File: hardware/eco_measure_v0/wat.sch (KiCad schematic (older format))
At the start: 31 parts

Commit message: desarrollando el hardware
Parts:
- removed C? (x6): 100nF, Capacitors_SMD:C_1206_HandSoldering, symbol wat-rescue:C
- removed D? (x2): D_Zener, symbol Device:D_Zener
- removed JP?: Jumper_2_Open, Jumper:SolderJumper-2_P1.3mm_Open_Pad1.0x1.5mm, symbol Jumper:Jumper_2_Open
- removed P?: PINZA_5, Connectors_Terminal_Blocks:TerminalBlock_bornier-2_P5.08mm, symbol wat-rescue:CONN_01X02
- removed P?: PINZA_6, Connectors_Terminal_Blocks:TerminalBlock_bornier-2_P5.08mm, symbol wat-rescue:CONN_01X02
- removed P?: PINZA_7, Connectors_Terminal_Blocks:TerminalBlock_bornier-2_P5.08mm, symbol wat-rescue:CONN_01X02
- removed P? (x2): PINZA_1, Connectors_Terminal_Blocks:TerminalBlock_bornier-2_P5.08mm, symbol wat-rescue:CONN_01X02
- removed P?: PINZA_2, Connectors_Terminal_Blocks:TerminalBlock_bornier-2_P5.08mm, symbol wat-rescue:CONN_01X02
- removed P?: PINZA_3, Connectors_Terminal_Blocks:TerminalBlock_bornier-2_P5.08mm, symbol wat-rescue:CONN_01X02
- removed P?: PINZA_4, Connectors_Terminal_Blocks:TerminalBlock_bornier-2_P5.08mm, symbol wat-rescue:CONN_01X02
- removed R? (x4): 10k, libreria_huellas_proyecto:Resistor_Horizontal_RM10mm, symbol wat-rescue:R
- removed R?: 2k2, libreria_huellas_proyecto:Resistor_Horizontal_RM10mm, symbol wat-rescue:R
- removed R?: 1k, libreria_huellas_proyecto:Resistor_Horizontal_RM10mm, symbol wat-rescue:R
- removed R?: 39, libreria_huellas_proyecto:Resistor_Horizontal_RM10mm, symbol wat-rescue:R
- removed R?: 10k, Resistors_SMD:R_1206_HandSoldering, symbol wat-rescue:R
- added C? (x16): 100nF, Capacitors_SMD:C_1206_HandSoldering, symbol wat-rescue:C
- added J? (x16): Conn_01x01, symbol Connector_Generic:Conn_01x01
- added R? (x26): 10k, libreria_huellas_proyecto:Resistor_Horizontal_RM10mm, symbol wat-rescue:R
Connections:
- net labels added: A0, D2
- net labels removed: 18b20_0, analogico_0, analogico_1, divisor_0, intensidad_1, lazo_0, pulsos_0, v_comun_0, v_comun_1, v_op, v_op_5v, v_referencia, voltage_1
- wire segments 127 -> 134
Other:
- moved on the sheet: C?, D?, J?, P?, U?, W?

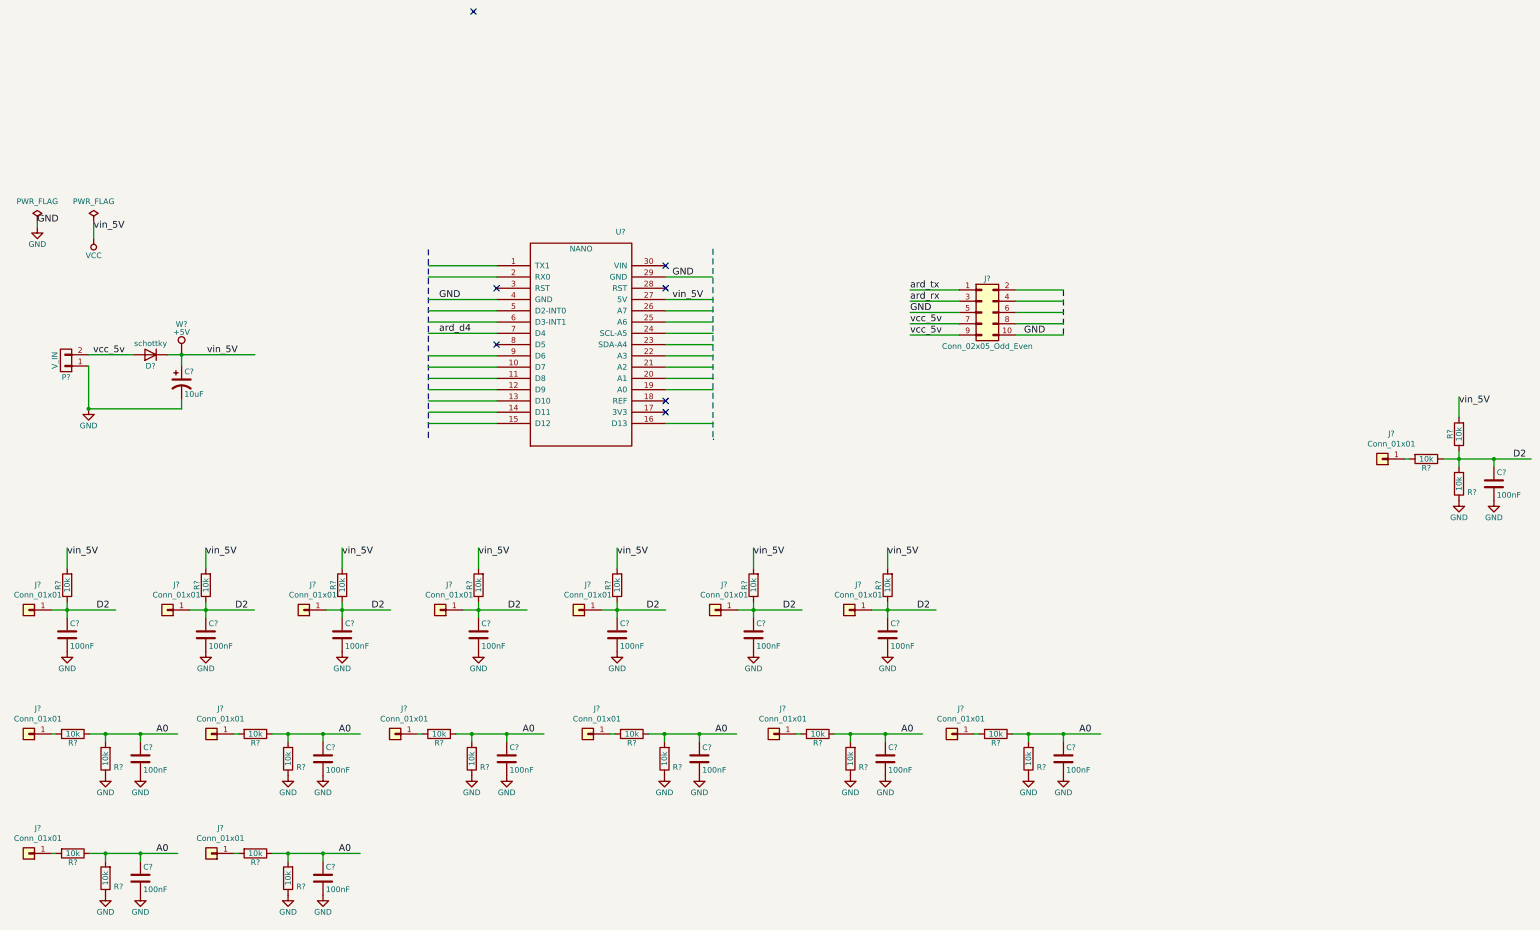
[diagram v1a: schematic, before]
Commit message: avanzando en la medida continua y la PCB
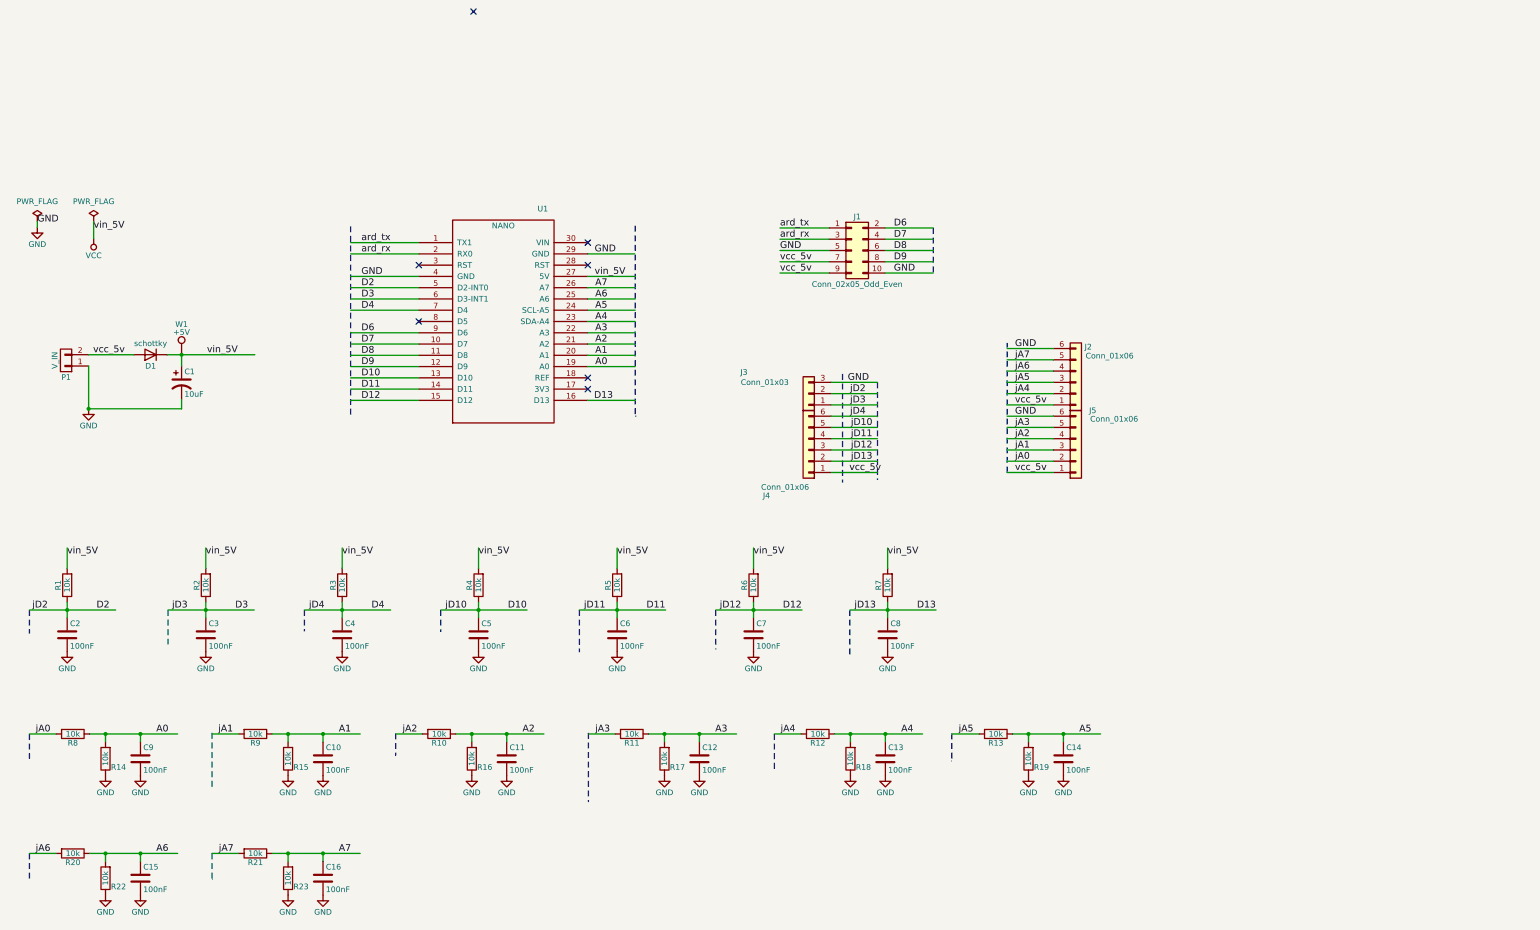
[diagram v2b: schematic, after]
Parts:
- removed C?: 100nF, Capacitors_SMD:C_1206_HandSoldering, symbol wat-rescue:C
- removed J? (x16): Conn_01x01, symbol Connector_Generic:Conn_01x01
- removed R? (x3): 10k, libreria_huellas_proyecto:Resistor_Horizontal_RM10mm, symbol wat-rescue:R
- added J2, J4, J5: Conn_01x06, TerminalBlock:TerminalBlock_bornier-6_P5.08mm, symbol Connector_Generic:Conn_01x06
- added J3: Conn_01x03, TerminalBlock:TerminalBlock_bornier-3_P5.08mm, symbol Connector_Generic:Conn_01x03
- C1: renamed from C?; footprint Capacitors_SMD:C_2220_HandSoldering -> eco_power_v2:C_2220_HandSoldering
- C10, C11, C12, C13, C14, C15, C16, C2, C3, C4, C5, C6, C7, C8, C9: renamed from C?; footprint Capacitors_SMD:C_1206_HandSoldering -> eco_power_v2:C_1206_HandSoldering
- D1: renamed from D?; footprint Diodes_SMD:D_2114 -> eco_power_v2:D_2114
- J1: renamed from J?; footprint oscar_libreria_huellas:Pin_Header_Straight_2x05_Pitch2.54mm_onsar -> eco_power_v2:Pin_Header_Straight_2x05_Pitch2.54mm_onsar
- P1: renamed from P?; footprint Connectors_Terminal_Blocks:TerminalBlock_bornier-2_P5.08mm -> eco_power_v2:TerminalBlock_bornier-2_P5.08mm
- R1, R10, R11, R12, R13, R14, R15, R16, R17, R18, R19, R2, R20, R21, R22, R23, R3, R4, R5, R6, R7, R8, R9: renamed from R?; footprint libreria_huellas_proyecto:Resistor_Horizontal_RM10mm -> eco_power_v2:R_1206_HandSoldering
- U1: renamed from U?; footprint libreria_huellas_proyecto:arduino_nano -> eco_power_v2:arduino_nano
- W1: renamed from W?; footprint Wire_Pads:SolderWirePad_single_0-8mmDrill -> eco_power_v2:SolderWirePad_single_0-8mmDrill
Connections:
- net labels added: A1, A2, A3, A4, A5, A6, A7, D10, D11, D12, D13, D3, D4, D6, D7, D8, D9, jA0, jA1, jA2, jA3, jA4, jA5, jA6, jA7, jD10, jD11, jD12, jD13, jD2, jD3, jD4
- net labels removed: ard_d4
- wire segments 134 -> 147
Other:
- moved on the sheet: J1, U1

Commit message: hw version operativa completa
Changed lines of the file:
@@
 Text Label 9680 2970 0    60   ~ 0
 jA1
-Text Label 9680 3170 0    60   ~ 0
-vcc_5v
 Text Label 9680 2670 0    60   ~ 0
 GND
-Text Label 9680 2570 0    60   ~ 0
-vcc_5v
 Text Label 9680 3070 0    60   ~ 0
 jA0
@@
 Wire Notes Line
 	8460 2370 8460 3235
-Text Label 8210 3170 0    60   ~ 0
-vcc_5v
 Wire Wire Line
 	8050 2670 8460 2670
@@
 	-1   0    0    1
 $EndComp
+Text Label 8210 3170 0    60   ~ 0
+vin_5V
+Text Label 9685 2570 0    60   ~ 0
+vin_5V
+Text Label 9685 3170 0    60   ~ 0
+vin_5V
 $EndSCHEMATC

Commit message: cambio de d13 por d5
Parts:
- U1: symbol nano1:NANO -> wat-rescue:NANO-nano1
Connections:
- net labels added: D5, jD5
- net labels removed: D13, jD13
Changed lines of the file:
@@
 Text Label 1500 2125 0    60   ~ 0
 vcc_5v
-$Comp
-L nano1:NANO U1
-U 1 1 5D4E51E2
-P 5140 1830
-F 0 "U1" H 5490 2830 50  0000 C CNN
-F 1 "NANO" H 5140 2680 50  0000 C CNN
-F 2 "eco_power_v2:arduino_nano" H 4840 1030 50  0001 C CNN
-F 3 "DOCUMENTATION" H 4990 980 50  0001 C CNN
-	1    5140 1830
-	1    0    0    -1
-$EndComp
 Text Label 5950 1430 0    60   ~ 0
 vin_5V
 NoConn ~ 4390 1330
-NoConn ~ 4390 1830
 NoConn ~ 5890 1130
 NoConn ~ 5890 1330
@@
 Wire Wire Line
 	4390 2530 3785 2530
-Wire Wire Line
-	5890 2530 6310 2530
 Wire Notes Line
 	8955 1000 8955 1400
@@
 	-1   0    0    -1
 $EndComp
-Text Label 6410 4390 0    60   ~ 0
+Text Label 7610 4390 0    60   ~ 0
 D11
 $Comp
@@
 	-1   0    0    -1
 $EndComp
-Text Label 7620 4390 0    60   ~ 0
+Text Label 8800 4390 0    60   ~ 0
 D12
 $Comp
@@
 	-1   0    0    -1
 $EndComp
-Text Label 8810 4390 0    60   ~ 0
-D13
 $Comp
 L wat-rescue:R R6
@@
 	-1   0    0    -1
 $EndComp
-Text Label 5180 4390 0    60   ~ 0
+Text Label 6405 4390 0    60   ~ 0
 D10
 $Comp
@@
 Text Label 3880 2530 0    60   ~ 0
 D12
-Text Label 5945 2530 0    60   ~ 0
-D13
 Text Label 5955 2230 0    60   ~ 0
 A0
@@
 jA5
 Text Label 8415 3070 2    60   ~ 0
-jD13
+jD12
 Wire Notes Line
 	935  4390 935  4600
@@
 jD4
 Text Label 5855 4390 0    60   ~ 0
+jD10
+Text Label 7060 4390 0    60   ~ 0
 jD11
-Text Label 7060 4390 0    60   ~ 0
+Text Label 8255 4390 0    60   ~ 0
 jD12
-Text Label 8255 4390 0    60   ~ 0
-jD13
 Text Label 4625 4390 0    60   ~ 0
-jD10
+jD5
 Wire Notes Line
 	8150 2295 8150 3260
@@
 	8050 3070 8460 3070
 Text Label 8415 2970 2    60   ~ 0
-jD12
+jD11
 Text Label 8415 2870 2    60   ~ 0
-jD11
-Text Label 8415 2770 2    60   ~ 0
 jD10
+Text Label 8360 2770 2    60   ~ 0
+jD5
 Text Label 8355 2670 2    60   ~ 0
 jD4
@@
 Text Label 9685 3170 0    60   ~ 0
 vin_5V
+NoConn ~ 5890 2530
+$Comp
+L wat-rescue:NANO-nano1 U1
+U 1 1 5D4E51E2
+P 5140 1830
+F 0 "U1" H 5490 2830 50  0000 C CNN
+F 1 "NANO" H 5140 2680 50  0000 C CNN
+F 2 "eco_power_v2:arduino_nano" H 4840 1030 50  0001 C CNN
+F 3 "DOCUMENTATION" H 4990 980 50  0001 C CNN
+	1    5140 1830
+	1    0    0    -1
+$EndComp
+Wire Wire Line
+	4390 1830 3785 1830
+Text Label 3880 1830 0    60   ~ 0
+D5
+Text Label 5235 4390 0    60   ~ 0
+D5
 $EndSCHEMATC
